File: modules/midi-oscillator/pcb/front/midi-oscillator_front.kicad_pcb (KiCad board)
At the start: 2 copper layers, 38.2 x 110.2 mm, 46 parts, among them J1 AudioJack3, J2 Conn_01x04, J3 CH1, J4 CH2, J5 CH3, J6 CH4, J7 Conn_01x14, SW1 Rotary_Encoder_Switch, U1 6N137, U2 TL071, U3 TL074

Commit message: modules: midi-oscillator: schematic improvements, added pdf
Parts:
- C4, C5, C6, C7: value 10n -> 4.7n
- C8, C9: value C -> 100n
- J1: value AudioJack3 -> Thonkiconn ST
- J2: value Conn_01x04 -> Pin Header 1x4
- J3: value CH1 -> Thonkiconn SM
- J4: value CH2 -> Thonkiconn SM
- J5: value CH3 -> Thonkiconn SM
- J6: value CH4 -> Thonkiconn SM
- J7: value Conn_01x14 -> Pin Header 1x14
- R1: value R -> 22k
- R10, R14, R18, R2, R6: value R -> 10k
- R11, R15, R19, R7: value R -> 39k
- R12, R16, R20, R8: value R -> 1k
- R13, R17, R5, R9: value R -> 560R
- SW1: value Rotary_Encoder_Switch -> PEC11R-4220K-S0024
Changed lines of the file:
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@@
   (page A4)
   (title_block
-    (title "midi-oscillator front board")
+    (title "midi-oscillator front")
     (date 2021-12-15)
     (rev 1.0)
@@
       (effects (font (size 1 1) (thickness 0.15)))
     )
-    (fp_text value R (at 5.08 2.37 90) (layer F.Fab)
+    (fp_text value 22k (at 5.08 2.37 90) (layer F.Fab)
       (effects (font (size 1 1) (thickness 0.15)))
     )
@@
       (effects (font (size 1 1) (thickness 0.15)))
     )
-    (fp_text value C (at 2.5 2.2 90) (layer F.Fab)
+    (fp_text value 100n (at 2.5 2.2 90) (layer F.Fab)
       (effects (font (size 1 1) (thickness 0.15)))
     )
@@
       (effects (font (size 1 1) (thickness 0.15)))
     )
-    (fp_text value C (at 2.5 2.2 90) (layer F.Fab)
+    (fp_text value 100n (at 2.5 2.2 90) (layer F.Fab)
       (effects (font (size 1 1) (thickness 0.15)))
     )
@@
       (effects (font (size 1 1) (thickness 0.15)))
     )
-    (fp_text value R (at 5.08 2.37 90) (layer F.Fab)
+    (fp_text value 560R (at 5.08 2.37 90) (layer F.Fab)
       (effects (font (size 1 1) (thickness 0.15)))
     )
@@
       (effects (font (size 1 1) (thickness 0.15)) (justify mirror))
     )
-    (fp_text value Conn_01x14 (at 0 -35.35) (layer B.Fab)
+    (fp_text value "Pin Header 1x14" (at 0 -35.35) (layer B.Fab)
       (effects (font (size 1 1) (thickness 0.15)) (justify mirror))
     )
@@
       (effects (font (size 1 1) (thickness 0.15)))
     )
-    (fp_text value Rotary_Encoder_Switch (at 7.5 10.4) (layer F.Fab)
+    (fp_text value PEC11R-4220K-S0024 (at 7.5 10.4) (layer F.Fab)
       (effects (font (size 1 1) (thickness 0.15)))
     )
@@
       (effects (font (size 1 1) (thickness 0.15)))
     )
-    (fp_text value R (at 5.08 2.37) (layer F.Fab)
+    (fp_text value 1k (at 5.08 2.37) (layer F.Fab)
       (effects (font (size 1 1) (thickness 0.15)))
     )
@@
       (effects (font (size 1 1) (thickness 0.15)))
     )
-    (fp_text value R (at 5.08 2.37 90) (layer F.Fab)
+    (fp_text value 39k (at 5.08 2.37 90) (layer F.Fab)
       (effects (font (size 1 1) (thickness 0.15)))
     )
@@
       (effects (font (size 1 1) (thickness 0.15)))
     )
-    (fp_text value R (at 5.08 2.37 90) (layer F.Fab)
+    (fp_text value 10k (at 5.08 2.37 90) (layer F.Fab)
       (effects (font (size 1 1) (thickness 0.15)))
     )
@@
       (effects (font (size 1 1) (thickness 0.15)))
     )
-    (fp_text value R (at 5.08 2.37 90) (layer F.Fab)
+    (fp_text value 560R (at 5.08 2.37 90) (layer F.Fab)
       (effects (font (size 1 1) (thickness 0.15)))
     )
@@
       (effects (font (size 1 1) (thickness 0.15)))
     )
-    (fp_text value R (at 5.08 2.37 90) (layer F.Fab)
+    (fp_text value 1k (at 5.08 2.37 90) (layer F.Fab)
       (effects (font (size 1 1) (thickness 0.15)))
     )
@@
       (effects (font (size 1 1) (thickness 0.15)))
     )
-    (fp_text value R (at 5.08 2.37 90) (layer F.Fab)
+    (fp_text value 39k (at 5.08 2.37 90) (layer F.Fab)
       (effects (font (size 1 1) (thickness 0.15)))
     )
@@
       (effects (font (size 1 1) (thickness 0.15)))
     )
-    (fp_text value R (at 5.08 2.37 90) (layer F.Fab)
+    (fp_text value 10k (at 5.08 2.37 90) (layer F.Fab)
       (effects (font (size 1 1) (thickness 0.15)))
     )
@@
       (effects (font (size 1 1) (thickness 0.15)))
     )
-    (fp_text value R (at 5.08 2.37 90) (layer F.Fab)
+    (fp_text value 560R (at 5.08 2.37 90) (layer F.Fab)
       (effects (font (size 1 1) (thickness 0.15)))
     )
@@
       (effects (font (size 1 1) (thickness 0.15)))
     )
-    (fp_text value R (at 5.08 2.37 90) (layer F.Fab)
+    (fp_text value 1k (at 5.08 2.37 90) (layer F.Fab)
       (effects (font (size 1 1) (thickness 0.15)))
     )
@@
       (effects (font (size 1 1) (thickness 0.15)))
     )
-    (fp_text value R (at 5.08 2.37 90) (layer F.Fab)
+    (fp_text value 39k (at 5.08 2.37 90) (layer F.Fab)
       (effects (font (size 1 1) (thickness 0.15)))
     )
@@
       (effects (font (size 1 1) (thickness 0.15)))
     )
-    (fp_text value R (at 5.08 2.37 90) (layer F.Fab)
+    (fp_text value 10k (at 5.08 2.37 90) (layer F.Fab)
       (effects (font (size 1 1) (thickness 0.15)))
     )
@@
       (effects (font (size 1 1) (thickness 0.15)))
     )
-    (fp_text value R (at 5.08 2.37) (layer F.Fab)
+    (fp_text value 1k (at 5.08 2.37) (layer F.Fab)
       (effects (font (size 1 1) (thickness 0.15)))
     )
@@
       (effects (font (size 1 1) (thickness 0.15)))
     )
-    (fp_text value R (at 5.08 2.37 90) (layer F.Fab)
+    (fp_text value 39k (at 5.08 2.37 90) (layer F.Fab)
       (effects (font (size 1 1) (thickness 0.15)))
     )
@@
       (effects (font (size 1 1) (thickness 0.15)))
     )
-    (fp_text value R (at 5.08 2.37 90) (layer F.Fab)
+    (fp_text value 10k (at 5.08 2.37 90) (layer F.Fab)
       (effects (font (size 1 1) (thickness 0.15)))
     )
@@
       (effects (font (size 1 1) (thickness 0.15)))
     )
-    (fp_text value R (at 5.08 2.37 90) (layer F.Fab)
+    (fp_text value 560R (at 5.08 2.37 90) (layer F.Fab)
       (effects (font (size 1 1) (thickness 0.15)))
     )
@@
       (effects (font (size 1 1) (thickness 0.15)))
     )
-    (fp_text value R (at 5.08 2.37) (layer F.Fab)
+    (fp_text value 10k (at 5.08 2.37) (layer F.Fab)
       (effects (font (size 1 1) (thickness 0.15)))
     )
@@
       (effects (font (size 1 1) (thickness 0.15)))
     )
-    (fp_text value CH4 (at 0 -5 90) (layer F.Fab)
+    (fp_text value "Thonkiconn SM" (at 0 -5 90) (layer F.Fab)
       (effects (font (size 1 1) (thickness 0.15)))
     )
@@
       (effects (font (size 1 1) (thickness 0.15)))
     )
-    (fp_text value CH3 (at 0 -5 90) (layer F.Fab)
+    (fp_text value "Thonkiconn SM" (at 0 -5 90) (layer F.Fab)
       (effects (font (size 1 1) (thickness 0.15)))
     )
@@
       (effects (font (size 1 1) (thickness 0.15)))
     )
-    (fp_text value CH2 (at 0 -5 90) (layer F.Fab)
+    (fp_text value "Thonkiconn SM" (at 0 -5 90) (layer F.Fab)
       (effects (font (size 1 1) (thickness 0.15)))
     )
@@
       (effects (font (size 1 1) (thickness 0.15)))
     )
-    (fp_text value CH1 (at 0 -5 90) (layer F.Fab)
+    (fp_text value "Thonkiconn SM" (at 0 -5 90) (layer F.Fab)
       (effects (font (size 1 1) (thickness 0.15)))
     )
@@
       (effects (font (size 1 1) (thickness 0.15)))
     )
-    (fp_text value Conn_01x04 (at 0 10.39 90) (layer F.Fab)
+    (fp_text value "Pin Header 1x4" (at 0 10.39 90) (layer F.Fab)
       (effects (font (size 1 1) (thickness 0.15)))
     )
@@
       (effects (font (size 1 1) (thickness 0.15)))
     )
-    (fp_text value AudioJack3 (at 0 -5) (layer F.Fab)
+    (fp_text value "Thonkiconn ST" (at 0 -5) (layer F.Fab)
       (effects (font (size 1 1) (thickness 0.15)))
     )
@@
       (effects (font (size 1 1) (thickness 0.15)))
     )
-    (fp_text value 10n (at 1.25 2.05) (layer F.Fab)
+    (fp_text value 4.7n (at 1.25 2.05) (layer F.Fab)
       (effects (font (size 1 1) (thickness 0.15)))
     )
@@
       (effects (font (size 1 1) (thickness 0.15)))
     )
-    (fp_text value 10n (at 1.25 2.05) (layer F.Fab)
+    (fp_text value 4.7n (at 1.25 2.05) (layer F.Fab)
       (effects (font (size 1 1) (thickness 0.15)))
     )
@@
       (effects (font (size 1 1) (thickness 0.15)))
     )
-    (fp_text value 10n (at 1.25 2.05) (layer F.Fab)
+    (fp_text value 4.7n (at 1.25 2.05) (layer F.Fab)
       (effects (font (size 1 1) (thickness 0.15)))
     )
@@
       (effects (font (size 1 1) (thickness 0.15)))
     )
-    (fp_text value 10n (at 1.25 2.05) (layer F.Fab)
-      (effects (font (size 1 1) (thickness 0.15)))
-    )
+    (fp_text value 4.7n (at 1.25 2.05) (layer F.Fab)
+      (effects (font (size 1 1) (thickness 0.15)))
+    )

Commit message: modules: midi-oscillator: front: upgrade to kicad 6
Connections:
- J1 pad S: (no net) -> unconnected-(J1-PadS)
- J3 pad TN: (no net) -> unconnected-(J3-PadTN)
- J4 pad TN: (no net) -> unconnected-(J4-PadTN)
- J5 pad TN: (no net) -> unconnected-(J5-PadTN)
- J6 pad TN: (no net) -> unconnected-(J6-PadTN)
- U1 pad 1: (no net) -> unconnected-(U1-Pad1)
- U1 pad 7: (no net) -> unconnected-(U1-Pad7)
- U2 pad 1: (no net) -> unconnected-(U2-Pad1)
- U2 pad 5: (no net) -> unconnected-(U2-Pad5)
- U2 pad 8: (no net) -> unconnected-(U2-Pad8)
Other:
- net class Default removed

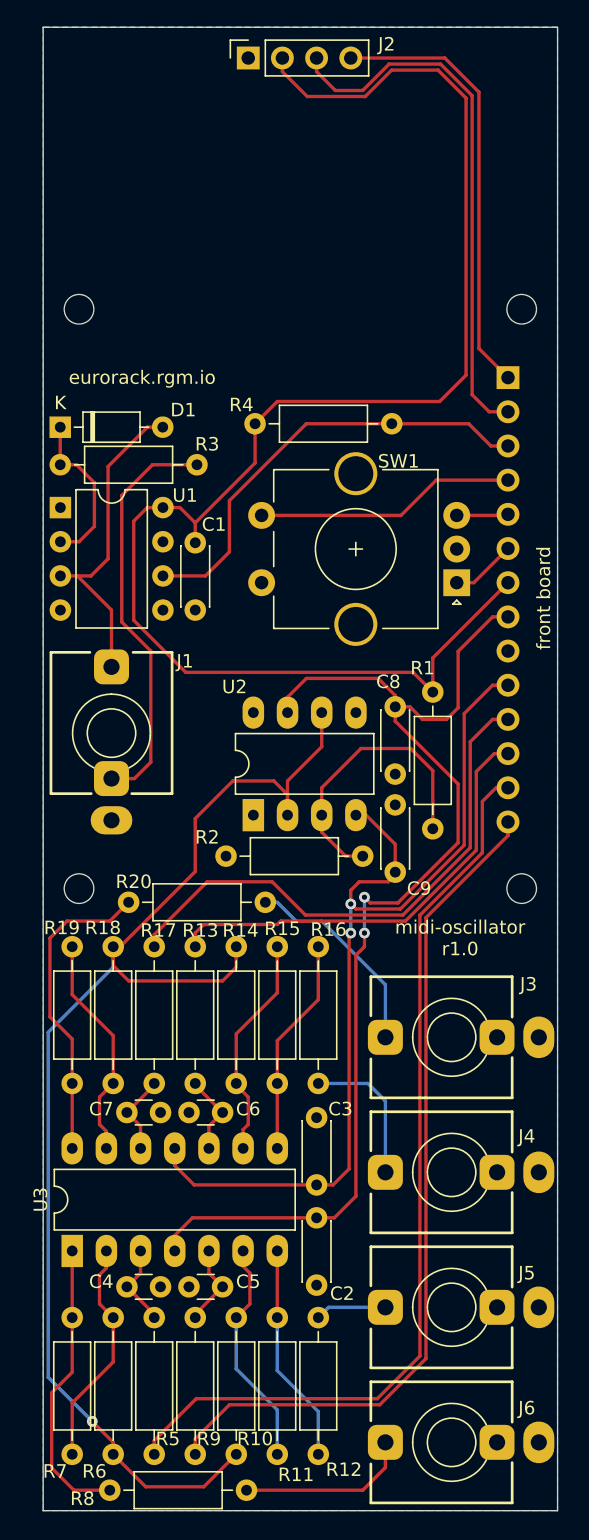
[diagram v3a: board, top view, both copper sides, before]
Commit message: modules: midi-oscillator: front: new revision 1.1
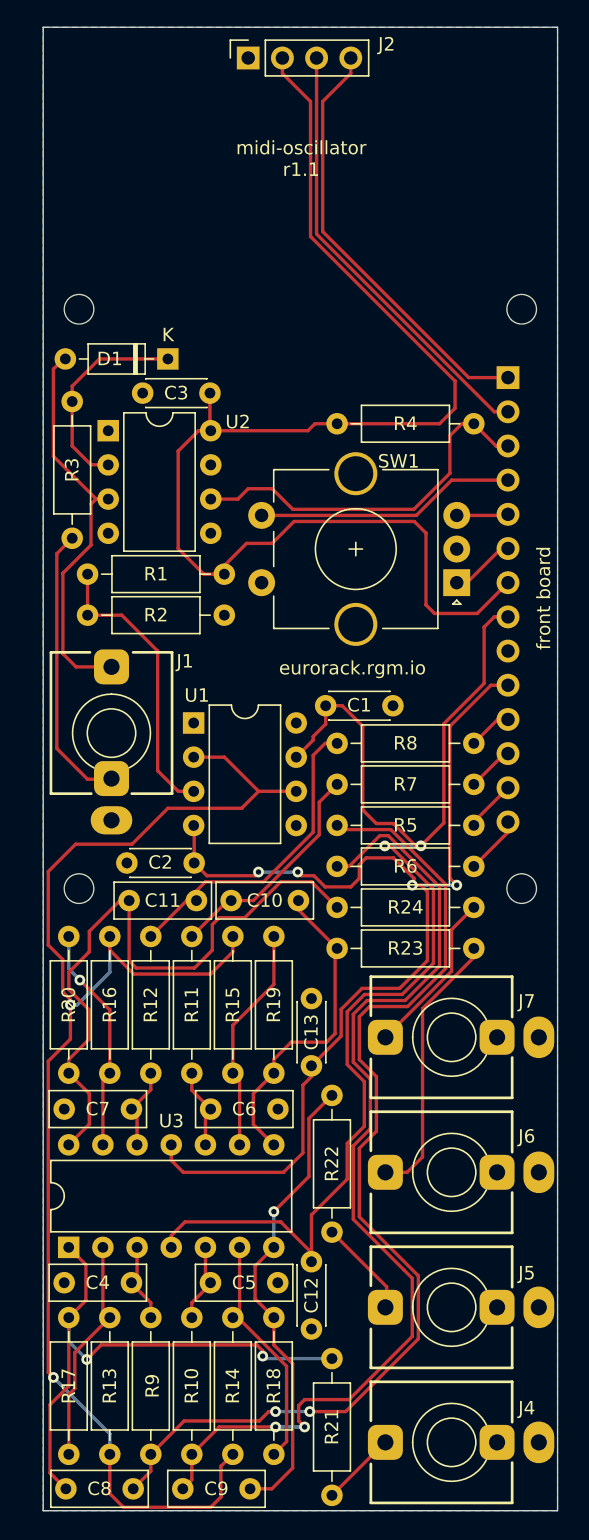
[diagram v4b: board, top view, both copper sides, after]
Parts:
- added C10: 4.7n, Capacitor_THT:C_Rect_L7.0mm_W2.5mm_P5.00mm, F.Cu at (128.1, 104.1)
- added C11: 4.7n, Capacitor_THT:C_Rect_L7.0mm_W2.5mm_P5.00mm, F.Cu at (125.6, 104.1)
- added C12: 100n, Capacitor_THT:C_Disc_D4.3mm_W1.9mm_P5.00mm, F.Cu at (134.1, 136.0)
- added C13: 100n, Capacitor_THT:C_Disc_D4.3mm_W1.9mm_P5.00mm, F.Cu at (134.1, 111.4)
- added R21: 1k, Resistor_THT:R_Axial_DIN0207_L6.3mm_D2.5mm_P10.16mm_Horizontal, F.Cu at (135.6, 148.3)
- added R22: 1k, Resistor_THT:R_Axial_DIN0207_L6.3mm_D2.5mm_P10.16mm_Horizontal, F.Cu at (135.6, 128.8)
- added R23: 1k, Resistor_THT:R_Axial_DIN0207_L6.3mm_D2.5mm_P10.16mm_Horizontal, F.Cu at (146.2, 107.7)
- added R24: 1k, Resistor_THT:R_Axial_DIN0207_L6.3mm_D2.5mm_P10.16mm_Horizontal, F.Cu at (146.2, 104.6)
- C2, C3: value C -> 100n
- C4, C5, C6, C7: footprint Capacitor_THT:C_Disc_D3.0mm_W1.6mm_P2.50mm -> Capacitor_THT:C_Rect_L7.0mm_W2.5mm_P5.00mm
- C8, C9: value 100n -> 4.7n; footprint Capacitor_THT:C_Disc_D4.3mm_W1.9mm_P5.00mm -> Capacitor_THT:C_Rect_L7.0mm_W2.5mm_P5.00mm
- R10, R6: value 10k -> 2k2
- R11, R7: value 39k -> 2k2
- R12, R8: value 1k -> 2k2
- R13: value 560R -> 10k
- R15: value 39k -> 10k
- R16: value 1k -> 10k
- R17: value 560R -> 39k
- R18: value 10k -> 39k
- R20: value 1k -> 39k
- R5, R9: value 560R -> 2k2
- SW1: value PEC11R-4220K-S0024 -> PEC11R-4215F-S0024
- U1: value 6N137 -> TL071
- U2: value TL071 -> 6N137; footprint Package_DIP:DIP-8_W7.62mm_LongPads -> Package_DIP:DIP-8_W7.62mm
- U3: footprint Package_DIP:DIP-14_W7.62mm_LongPads -> Package_DIP:DIP-14_W7.62mm
- moved C8 56.6 mm to (120.9, 147.9), turned to 180 degrees
- moved R8 55.9 mm to (136.0, 92.5), turned to 0 degrees
- moved C3 55.4 mm to (121.6, 66.4), turned to 0 degrees
- moved C9 53.2 mm to (124.6, 147.9), turned to 0 degrees
- moved R7 44.2 mm to (136.0, 95.5), turned to 0 degrees
- moved R5 39.0 mm to (136.0, 98.6), turned to 0 degrees
- moved R6 37.4 mm to (136.0, 101.6), turned to 0 degrees
- moved C2 34.4 mm to (120.4, 101.3), turned to 0 degrees
- moved U2 30.5 mm to (119.0, 69.2), turned to 0 degrees
- moved R2 27.2 mm to (117.5, 82.9), turned to 0 degrees
- moved R12 22.0 mm to (122.2, 117.0), turned to 90 degrees
- moved R18 21.1 mm to (131.3, 135.1), turned to -90 degrees
- moved R20 19.4 mm to (116.1, 117.0), turned to 90 degrees
- moved R11 19.2 mm to (125.2, 117.0), turned to 90 degrees
- moved U1 18.8 mm to (125.4, 90.9)
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- renumbered J7 to J3, J6 to J4, J4 to J6, J3 to J7
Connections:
- C1 pad 2: +3V3 -> +12V
- C2 pad 2: +12V -> -12V
- C3 pad 2: -12V -> +3.3V
- C8 pad 1: GND -> Net-(C8-Pad1)
- C8 pad 2: +12V -> Net-(C8-Pad2)
- C9 pad 1: GND -> Net-(C9-Pad1)
- C9 pad 2: -12V -> Net-(C9-Pad2)
- J2 pad 2: +3V3 -> +3.3V
- J3 pad 7: +3V3 -> +3.3V
- J4 pad T: Net-(J6-PadT) -> Net-(J4-PadT)
- J6 pad T: Net-(J4-PadT) -> Net-(J6-PadT)
- J7 pad T: Net-(J3-PadT) -> Net-(J7-PadT)
- R1 pad 1: +3V3 -> +3.3V
- R10 pad 1: Net-(R10-Pad1) -> Net-(C5-Pad1)
- R10 pad 2: VREF -> Net-(C9-Pad1)
- R11 pad 1: Net-(R11-Pad1) -> Net-(C6-Pad1)
- R11 pad 2: Net-(R10-Pad1) -> Net-(C10-Pad1)
- R12 pad 1: Net-(J5-PadT) -> Net-(C7-Pad1)
- R12 pad 2: Net-(R11-Pad1) -> Net-(C11-Pad1)
- R13 pad 1: Net-(C6-Pad1) -> Net-(R13-Pad1)
- R13 pad 2: DAC_CH2 -> VREF
- R15 pad 2: Net-(R14-Pad1) -> VREF
- R16 pad 1: Net-(J4-PadT) -> Net-(R16-Pad1)
- R16 pad 2: Net-(R15-Pad1) -> VREF
- R17 pad 1: Net-(C7-Pad1) -> Net-(C8-Pad2)
- R17 pad 2: DAC_CH1 -> Net-(R13-Pad1)
- R18 pad 1: Net-(R18-Pad1) -> Net-(C9-Pad2)
- R18 pad 2: VREF -> Net-(R14-Pad1)
- R19 pad 1: Net-(R19-Pad1) -> Net-(C10-Pad2)
- R19 pad 2: Net-(R18-Pad1) -> Net-(R15-Pad1)
- R20 pad 1: Net-(J3-PadT) -> Net-(C11-Pad2)
- R20 pad 2: Net-(R19-Pad1) -> Net-(R16-Pad1)
- R4 pad 1: +3V3 -> +3.3V
- R5 pad 1: Net-(C4-Pad1) -> Net-(C8-Pad1)
- R6 pad 1: Net-(R6-Pad1) -> Net-(C9-Pad1)
- R6 pad 2: VREF -> DAC_CH3
- R7 pad 1: Net-(R7-Pad1) -> Net-(C10-Pad1)
- R7 pad 2: Net-(R6-Pad1) -> DAC_CH2
- R8 pad 1: Net-(J6-PadT) -> Net-(C11-Pad1)
- R8 pad 2: Net-(R7-Pad1) -> DAC_CH1
- R9 pad 1: Net-(C5-Pad1) -> Net-(C4-Pad1)
- R9 pad 2: DAC_CH3 -> Net-(C8-Pad1)
- U1 pad 2: Net-(D1-Pad1) -> VREF
- U1 pad 3: Net-(D1-Pad2) -> Net-(R1-Pad2)
- U1 pad 4: (no net) -> -12V
- U1 pad 5: GND -> unconnected-(U1-Pad5)
- U1 pad 6: MIDI_RX -> VREF
- U1 pad 7: unconnected-(U1-Pad7) -> +12V
- U1 pad 8: +3V3 -> unconnected-(U1-Pad8)
- U2 pad 2: VREF -> Net-(D1-Pad1)
- U2 pad 3: Net-(R1-Pad2) -> Net-(D1-Pad2)
- U2 pad 4: -12V -> (no net)
- U2 pad 5: unconnected-(U2-Pad5) -> GND
- U2 pad 6: VREF -> MIDI_RX
- U2 pad 7: +12V -> unconnected-(U2-Pad7)
- U2 pad 8: unconnected-(U2-Pad8) -> +3.3V
- U3 pad 1: Net-(R7-Pad1) -> Net-(C8-Pad2)
- U3 pad 13: Net-(R18-Pad1) -> Net-(R16-Pad1)
- U3 pad 14: Net-(R19-Pad1) -> Net-(C11-Pad2)
- U3 pad 2: Net-(R6-Pad1) -> Net-(R13-Pad1)
- U3 pad 6: Net-(R10-Pad1) -> Net-(R14-Pad1)
- U3 pad 7: Net-(R11-Pad1) -> Net-(C9-Pad2)
- U3 pad 8: Net-(R15-Pad1) -> Net-(C10-Pad2)
- U3 pad 9: Net-(R14-Pad1) -> Net-(R15-Pad1)
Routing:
- net +3V3: track 113.3 -> 0.00 mm
- net +3.3V: track 0.00 -> 97.5 mm
- net Net-(C8-Pad1): track 0.00 -> 77.4 mm, vias 0 -> 2
- net Net-(C9-Pad1): track 0.00 -> 75.1 mm, vias 0 -> 2
- net DAC_CH4: track 68.8 -> 3.85 mm
- net DAC_CH3: track 63.2 -> 4.35 mm
- net Net-(C11-Pad2): track 0.00 -> 47.6 mm
- net Net-(C8-Pad2): track 0.00 -> 43.0 mm, vias 0 -> 2
- net DAC_CH1: track 40.5 -> 3.28 mm
- net Net-(C9-Pad2): track 0.00 -> 35.0 mm, vias 0 -> 1
- net DAC_CH2: track 33.2 -> 3.49 mm
- net Net-(C10-Pad2): track 0.00 -> 24.1 mm
- net Net-(C11-Pad1): track 0.00 -> 23.6 mm
- net Net-(R19-Pad1): track 23.3 -> 0.00 mm
- net Net-(R7-Pad1): track 21.8 -> 0.00 mm
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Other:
- board text added: "midi-oscillator r1.1"
- board text removed: "midi-oscillator r1.0"
